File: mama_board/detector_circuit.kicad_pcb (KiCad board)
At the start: 4 copper layers, 94 x 99.1 mm, 123 parts, among them J1 Programming Header, J2 CAN Header, J3 BATT_1, J4 BATT_2, J5 BATT_3, J6 BATT_4, J7 TEST_CONN, J8 693072010801, J9 SIPM_CONN, Q1 BSS138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

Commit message: Addressed Jack's Comments, got half of Chamath's comments addressed
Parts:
- removed J2: CAN Header, Connector_PinHeader_2.54mm:PinHeader_1x05_P2.54mm_Vertical
- removed REF** (x4): MountingHole_3.5mm, MountingHole:MountingHole_3.5mm
- added J10: Conn_01x06_Female, canhw_footprints:connector_Harwin_M80-5000642, F.Cu at (105.0, 54.1)
- JP5: value TRANS_OUT -> TRANS_JUMP
- TP1: value PEAK OUT -> PEAK_OUT
- U3: footprint Package_TO_SOT_SMD:SOT-23-5_HandSoldering -> Package_TO_SOT_SMD:TSOT-23-5_HandSoldering
- moved L1 2.19 mm to (165.2, 100.6)
- moved C15 2.05 mm to (166.0, 106.9)
- moved C16 2.05 mm to (166.0, 109.9)
- moved D1 2.05 mm to (169.7, 105.4)
- moved C7 1.91 mm to (170.2, 100.6)
- moved R11 1.53 mm to (161.9, 111.6)
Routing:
- net +BATT: track 60.3 -> 38.3 mm
- net Net-(C7-Pad1): track 58.3 -> 42.0 mm
- net GND: track 203.8 -> 189.5 mm, vias 123 -> 127
- net +37V: track 32.7 -> 24.4 mm
- net /Microcontroller [DO NOT PLACE]/CANL: track 12.3 -> 8.32 mm
- net Net-(D1-Pad2): track 10.6 -> 12.1 mm
- net /Microcontroller [DO NOT PLACE]/CANH: track 7.13 -> 5.78 mm, vias 0 -> 1
- net Net-(R11-Pad1): track 6.55 -> 5.42 mm
- net Net-(J8-Pad3): track 15.4 -> 16.3 mm
- net Net-(C18-Pad2): track 35.2 -> 36.0 mm
- net Net-(R28-Pad2): track 23.5 -> 22.9 mm
- net +5V: track 91.9 -> 91.7 mm, vias 12 -> 15
- added copper zone on F.Cu, net +4.7V
- added copper zone on F.Cu, net +5V
- added copper zone on F.Cu, net +BATT
- added copper zone on F.Cu, net Net-(C7-Pad1)
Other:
- board text added: "CAN Header"

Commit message: Finished Addressing chamath's Reviews
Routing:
- net /AMP_OUT: track 46.1 -> 36.0 mm
- net +4.7V: track 80.1 -> 82.0 mm
- net GND: track 189.5 -> 191.1 mm
- added copper zone on F.Cu, net /AMP_OUT

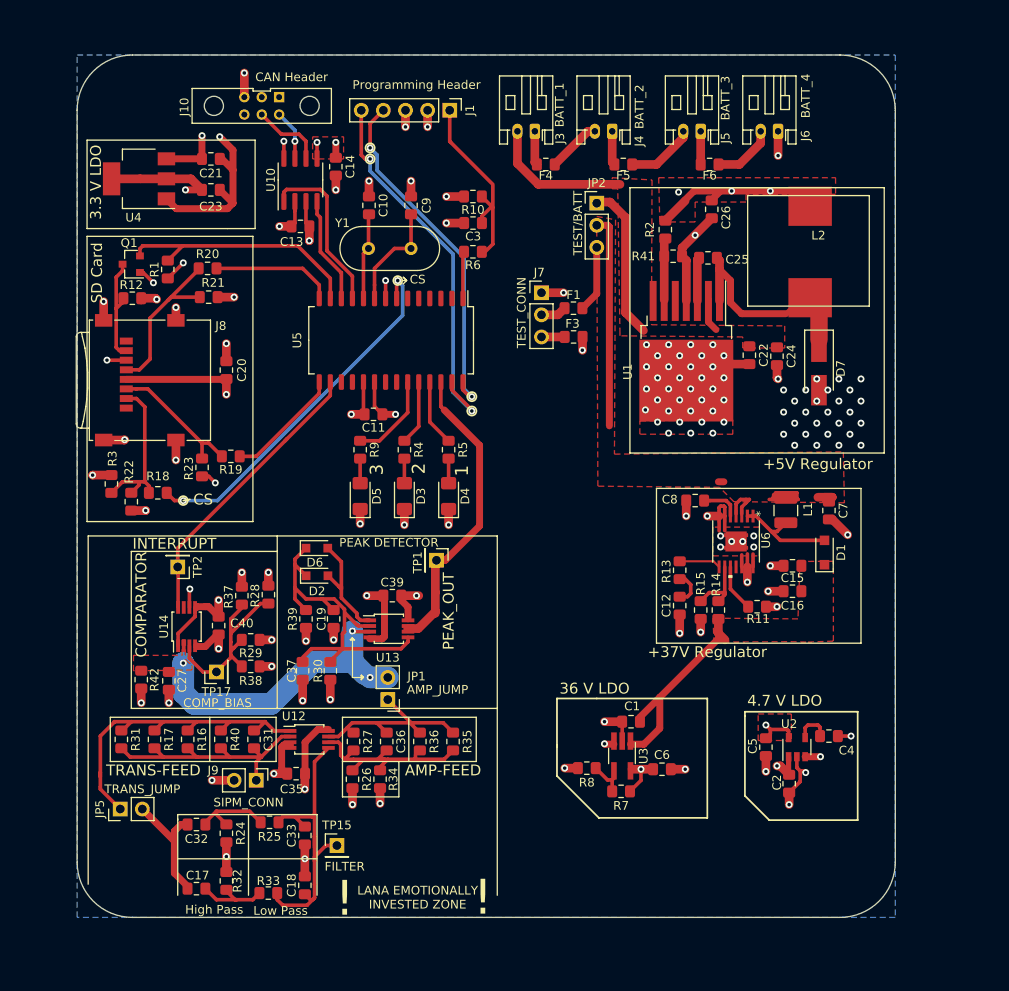
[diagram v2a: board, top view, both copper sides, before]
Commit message: added ground plane
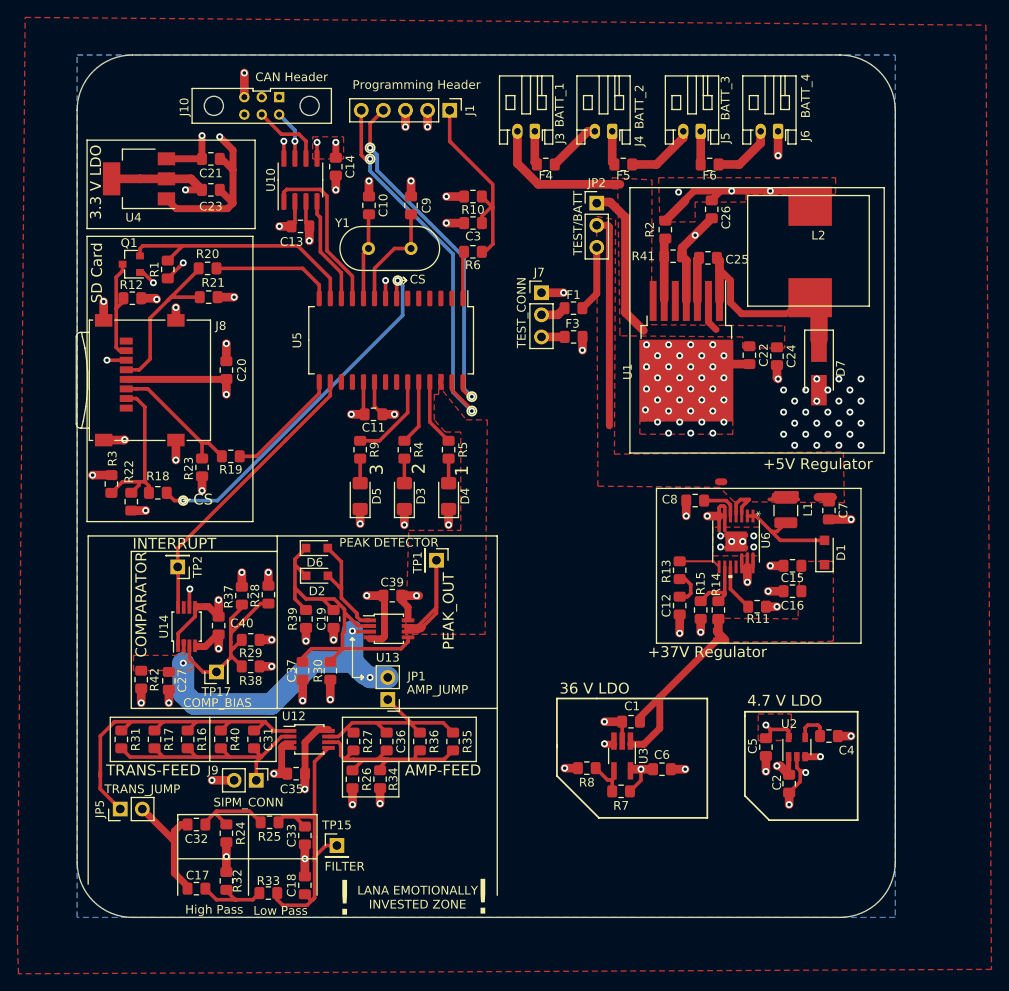
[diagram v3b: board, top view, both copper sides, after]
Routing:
- net /DET_ADC: track 35.0 -> 21.6 mm
- net +5V: track 91.7 -> 93.2 mm
- net GND: track 191.1 -> 190.5 mm
- added copper zone on F.Cu, net /DET_ADC
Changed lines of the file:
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@@
     (thickness 1.6)
     (drawings 110)
-    (tracks 881)
+    (tracks 879)
     (zones 0)
     (modules 119)
@@
   (layers
     (0 Papa.Cu signal)
-    (1 GND.Cu power hide)
-    (2 VCC.Cu power hide)
+    (1 GND.Cu power)
+    (2 VCC.Cu power)
     (31 Mama.Cu signal)
     (32 B.Adhes user hide)
@@
   )
   (setup
-    (last_trace_width 1)
+    (last_trace_width 0.8)
     (user_trace_width 0.42)
     (user_trace_width 0.8)
@@
   (via (at 144.399 124.841) (size 0.8) (drill 0.4) (layers Papa.Cu Mama.Cu) (net 1))
   (via (at 91.694 100.584) (size 0.8) (drill 0.4) (layers Papa.Cu Mama.Cu) (net 1))
-  (via (at 99.695 97.409) (size 0.8) (drill 0.4) (layers Papa.Cu Mama.Cu) (net 1))
-  (segment (start 98.171 96.656) (end 98.942 96.656) (width 0.42) (layer Papa.Cu) (net 1))
-  (segment (start 98.942 96.656) (end 99.695 97.409) (width 0.42) (layer Papa.Cu) (net 1))
+  (via (at 98.171 98.298) (size 0.8) (drill 0.4) (layers Papa.Cu Mama.Cu) (net 1))
   (via (at 100.965 81.407) (size 0.8) (drill 0.4) (layers Papa.Cu Mama.Cu) (net 1))
   (via (at 101.854 76.073) (size 0.8) (drill 0.4) (layers Papa.Cu Mama.Cu) (net 1))
@@
   (segment (start 166.878 131.717) (end 165.608 132.987) (width 0.42) (layer Papa.Cu) (net 1))
   (segment (start 166.878 130.498602) (end 166.878 131.717) (width 0.42) (layer Papa.Cu) (net 1))
-  (segment (start 171.205 126.492) (end 172.72 126.492) (width 0.42) (layer Papa.Cu) (net 1))
   (segment (start 144.399 124.841) (end 146.422 124.841) (width 1) (layer Papa.Cu) (net 1))
   (segment (start 121.412 100.4205) (end 121.412 102.235) (width 1) (layer Papa.Cu) (net 1))
@@
   (segment (start 108.839 65.086) (end 108.839 66.167) (width 0.42) (layer Papa.Cu) (net 1))
   (via (at 164.211 111.633) (size 0.8) (drill 0.4) (layers Papa.Cu Mama.Cu) (net 1))
-  (segment (start 170.18 101.609) (end 170.57 101.609) (width 1) (layer Papa.Cu) (net 1))
-  (segment (start 170.57 101.609) (end 172.339 103.378) (width 1) (layer Papa.Cu) (net 1))
-  (segment (start 172.339 103.378) (end 172.339 103.378) (width 1) (layer Papa.Cu) (net 1))
-  (via (at 172.339 103.378) (size 0.8) (drill 0.4) (layers Papa.Cu Mama.Cu) (net 1))
   (segment (start 162.95 111.633) (end 164.211 111.633) (width 1) (layer Papa.Cu) (net 1))
   (via (at 167.513 130.683) (size 0.8) (drill 0.4) (layers Papa.Cu Mama.Cu) (net 1))
@@
   (segment (start 94.361 121.176) (end 94.361 122.682) (width 1) (layer Papa.Cu) (net 1))
   (segment (start 100.076 114.826) (end 100.076 116.459) (width 1) (layer Papa.Cu) (net 1))
+  (segment (start 98.171 96.656) (end 98.171 98.298) (width 1) (layer Papa.Cu) (net 1))
+  (segment (start 170.18 101.609) (end 172.729 101.609) (width 1) (layer Papa.Cu) (net 1))
+  (segment (start 172.729 101.609) (end 172.729 101.609) (width 1) (layer Papa.Cu) (net 1))
+  (via (at 172.729 101.609) (size 0.8) (drill 0.4) (layers Papa.Cu Mama.Cu) (net 1))
+  (segment (start 171.205 126.492) (end 172.72 126.492) (width 1) (layer Papa.Cu) (net 1))
   (via (at 96.012 72.136) (size 0.8) (drill 0.4) (layers Papa.Cu Mama.Cu) (net 2))
   (via (at 98.171 57.531) (size 0.8) (drill 0.4) (layers Papa.Cu Mama.Cu) (net 2))
@@
   (segment (start 117.983 85.826) (end 117.983 88.628) (width 0.42) (layer Papa.Cu) (net 2))
   (segment (start 120.396 89.535) (end 120.396 89.535) (width 0.42) (layer Papa.Cu) (net 2))
-  (via (at 120.396 89.535) (size 0.8) (drill 0.4) (layers Papa.Cu Mama.Cu) (net 2))
+  (via (at 120.269 89.535) (size 0.8) (drill 0.4) (layers Papa.Cu Mama.Cu) (net 2))
   (segment (start 141.877 80.645) (end 141.877 82.187) (width 1) (layer Papa.Cu) (net 2))
   (segment (start 98.148 60.184) (end 98.162 60.198) (width 0.8) (layer Papa.Cu) (net 2))
@@
   (segment (start 163.449 63.881) (end 159.004 63.881) (width 0.8) (layer Papa.Cu) (net 2))
   (via (at 163.449 63.881) (size 0.8) (drill 0.4) (layers Papa.Cu Mama.Cu) (net 2))
+  (segment (start 120.307854 89.535) (end 120.351927 89.490927) (width 1) (layer Papa.Cu) (net 2))
+  (segment (start 118.89 89.535) (end 120.307854 89.535) (width 1) (layer Papa.Cu) (net 2))
   (segment (start 130.311 70.866) (end 130.683 70.866) (width 0.42) (layer Papa.Cu) (net 3))
   (segment (start 130.683 70.866) (end 131.572 69.977) (width 0.42) (layer Papa.Cu) (net 3))
@@
   (segment (start 101.473 114.681) (end 101.473 115.697) (width 0.42) (layer Papa.Cu) (net 53))
   (segment (start 101.473 113.03) (end 101.473 114.681) (width 0.42) (layer Papa.Cu) (net 53))
-  (segment (start 130.048 93.091) (end 125.984 89.027) (width 0.8) (layer Papa.Cu) (net 54))
-  (segment (start 125.603 88.646) (end 125.984 89.027) (width 0.42) (layer Papa.Cu) (net 54))
-  (segment (start 125.603 85.826) (end 125.603 88.646) (width 0.42) (layer Papa.Cu) (net 54))
-  (segment (start 124.968 106.426) (end 125.095 106.299) (width 1) (layer Papa.Cu) (net 54))
-  (segment (start 124.968 109.982) (end 124.968 106.426) (width 1) (layer Papa.Cu) (net 54))
-  (segment (start 124.968 109.982) (end 124.968 112.394) (width 1) (layer Papa.Cu) (net 54))
-  (segment (start 125.095 106.299) (end 126.111 106.299) (width 0.8) (layer Papa.Cu) (net 54))
-  (segment (start 130.048 102.362) (end 130.048 93.091) (width 0.8) (layer Papa.Cu) (net 54))
-  (segment (start 126.111 106.299) (end 130.048 102.362) (width 0.8) (layer Papa.Cu) (net 54))
-  (segment (start 124.991999 112.167801) (end 123.063 114.0968) (width 1) (layer Papa.Cu) (net 54))
-  (segment (start 122.9868 114.1476) (end 121.781799 114.1476) (width 1) (layer Papa.Cu) (net 54))
+  (segment (start 125.095 111.732) (end 125.095 106.299) (width 0.42) (layer Papa.Cu) (net 54))
+  (segment (start 122.979 113.848) (end 125.095 111.732) (width 0.42) (layer Papa.Cu) (net 54))
+  (segment (start 121.834 113.848) (end 122.979 113.848) (width 0.42) (layer Papa.Cu) (net 54))
+  (segment (start 125.095 112.382) (end 125.095 106.299) (width 0.42) (layer Papa.Cu) (net 54))
+  (segment (start 121.834 114.498) (end 122.979 114.498) (width 0.42) (layer Papa.Cu) (net 54))
+  (segment (start 123.501 113.976) (end 123.304 114.173) (width 0.8) (layer Papa.Cu) (net 54))
+  (segment (start 122.979 114.498) (end 123.501 113.976) (width 0.42) (layer Papa.Cu) (net 54))
+  (segment (start 123.501 113.976) (end 125.095 112.382) (width 0.42) (layer Papa.Cu) (net 54))
+  (segment (start 123.304 114.173) (end 121.793 114.173) (width 0.8) (layer Papa.Cu) (net 54))
   (segment (start 111.379 66.548) (end 111.379 65.086) (width 0.42) (layer Papa.Cu) (net 55))
   (segment (start 111.76 66.929) (end 111.379 66.548) (width 0.42) (layer Papa.Cu) (net 55))
@@
     )
   )
-  (zone (net 1) (net_name GND) (layer GND.Cu) (hatch edge 0.508)
-    (priority 2)
-    (connect_pads yes (clearance 0))
-    (min_thickness 0.254)
-    (fill yes (arc_segments 16) (thermal_gap 0.508) (thermal_bridge_width 0.508))
-    (polygon
-      (pts
-        (xy 179.07 148.59) (xy 81.28 148.59) (xy 81.28 46.99) (xy 179.07 45.72)
-      )
-    )
-  )
   (zone (net 2) (net_name +5V) (layer VCC.Cu) (hatch edge 0.508)
     (priority 2)
@@
   )
   (zone (net 1) (net_name GND) (layer Mama.Cu) (hatch edge 0.508)
-    (priority 2)
+    (priority 4)
     (connect_pads yes (clearance 0))
     (min_thickness 0.254)
@@
   )
   (zone (net 61) (net_name /AMP_OUT) (layer Papa.Cu) (hatch edge 0.508)
+    (priority 1)
     (connect_pads yes (clearance 0))
     (min_thickness 0.254)
@@
       )
     )
+  )
+  (zone (net 54) (net_name /DET_ADC) (layer Papa.Cu) (hatch edge 0.508)
+    (priority 1)
+    (connect_pads yes (clearance 0))
+    (min_thickness 0.254)
+    (fill yes (arc_segments 32) (thermal_gap 0.508) (thermal_bridge_width 0.508) (smoothing fillet) (radius 2))
+    (polygon
+      (pts
+        (xy 125.857 86.868) (xy 128.524 90.17) (xy 130.937 90.17) (xy 130.683 114.808) (xy 121.539 114.808)
+        (xy 121.92 102.87) (xy 127.889 102.87) (xy 127.889 91.567) (xy 126.111 91.567) (xy 124.841 90.17)
+        (xy 124.841 87.249) (xy 125.349 87.249) (xy 125.349 84.963) (xy 125.857 84.963)
+      )
+    )
+  )
+  (zone (net 1) (net_name GND) (layer GND.Cu) (hatch edge 0.508)
+    (connect_pads yes (clearance 0))
+    (min_thickness 0.254)
+    (fill yes (arc_segments 16) (thermal_gap 0.508) (thermal_bridge_width 0.508))
+    (polygon
+      (pts
+        (xy 179.705 150.241) (xy 82.042 150.241) (xy 82.423 47.371) (xy 179.197 47.371)
+      )
+    )
+  )
+  (zone (net 1) (net_name GND) (layer Papa.Cu) (hatch edge 0.508)
+    (connect_pads yes (clearance 0))
+    (min_thickness 0.254)
+    (fill yes (arc_segments 16) (thermal_gap 0.508) (thermal_bridge_width 0.508))
+    (polygon
+      (pts
+        (xy 188.214 44.831) (xy 188.849 153.289) (xy 77.089 153.797) (xy 76.962 149.987) (xy 77.851 43.942)
+      )
+    )

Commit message: addressed dawson & randy's comments, with the exception of team logo cause im having trouble
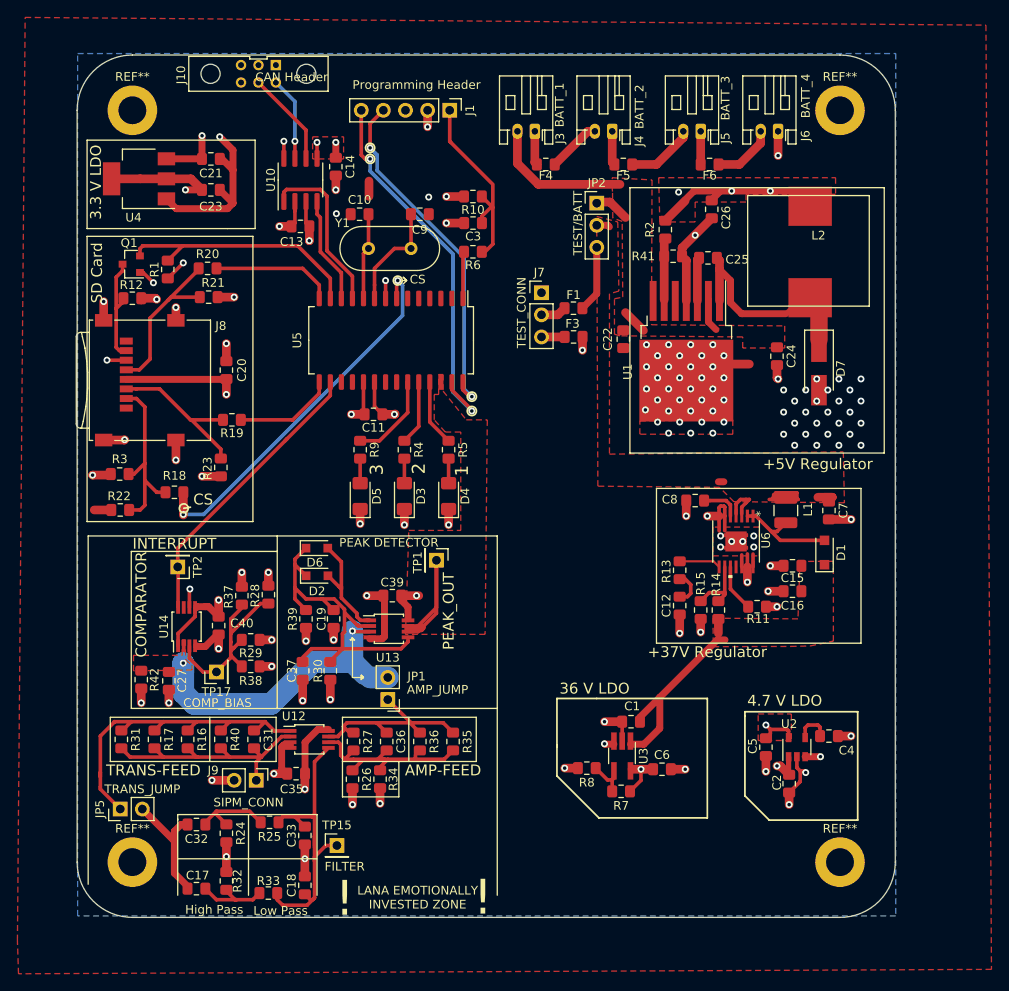
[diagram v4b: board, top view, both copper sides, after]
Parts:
- added REF**: MountingHole_3.2mm_M3_ISO7380_Pad, MountingHole:MountingHole_3.2mm_M3_ISO7380_Pad, F.Cu at (90.2, 54.6)
- added REF**: MountingHole_3.2mm_M3_ISO7380_Pad, MountingHole:MountingHole_3.2mm_M3_ISO7380_Pad, F.Cu at (171.4, 54.6)
- added REF**: MountingHole_3.2mm_M3_ISO7380_Pad, MountingHole:MountingHole_3.2mm_M3_ISO7380_Pad, F.Cu at (171.4, 141.0)
- added REF**: MountingHole_3.2mm_M3_ISO7380_Pad, MountingHole:MountingHole_3.2mm_M3_ISO7380_Pad, F.Cu at (90.2, 141.0)
- moved C22 14.6 mm to (146.6, 80.9)
- moved R19 4.19 mm to (101.6, 90.2)
- moved J10 3.70 mm to (104.6, 50.4)
- moved R23 2.16 mm to (100.3, 95.6)
- moved R18 1.91 mm to (95.0, 98.5)
- moved R22 1.59 mm to (88.8, 100.5), turned to 180 degrees
- moved R3 1.49 mm to (88.7, 96.4), turned to 0 degrees
- moved C10 1.48 mm to (116.3, 66.5), turned to 180 degrees
- moved C9 1.44 mm to (123.2, 66.5), turned to 0 degrees
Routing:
- net Net-(C7-Pad1): track 42.0 -> 19.1 mm
- net +BATT: track 38.3 -> 27.4 mm
- net GND: track 190.5 -> 181.8 mm, vias 127 -> 123
- net /Microcontroller [DO NOT PLACE]/CANH: track 5.78 -> 9.62 mm
- net /Microcontroller [DO NOT PLACE]/CANL: track 8.32 -> 11.0 mm
- net Net-(J8-Pad2): track 18.6 -> 21.2 mm
- net Net-(J8-Pad3): track 16.3 -> 18.4 mm
- net /Microcontroller [DO NOT PLACE]/MISO: track 42.5 -> 40.7 mm
- net +37V: track 24.4 -> 23.3 mm
- net /Microcontroller [DO NOT PLACE]/CS: track 42.6 -> 43.6 mm
- net Net-(C36-Pad1): track 23.3 -> 24.1 mm
- net /AMP_OUT: vias 3 -> 2

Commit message: Addressed Jared's comments
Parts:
- removed the REF** at (90.2, 54.6)
- removed the REF** at (171.4, 54.6)
- removed the REF** at (171.4, 141.0)
- removed the REF** at (90.2, 141.0)
- added G***: LOGO, Team_Logo:Logo_SilkScreen_15mm, F.Cu at (125.0, 137.7)
- added REF**: MountingHole_3.5mm_Pad, MountingHole:MountingHole_3.5mm_Pad, F.Cu at (90.2, 141.0)
- added REF**: MountingHole_3.5mm_Pad, MountingHole:MountingHole_3.5mm_Pad, F.Cu at (90.2, 54.6)
- added REF**: MountingHole_3.5mm_Pad, MountingHole:MountingHole_3.5mm_Pad, F.Cu at (171.4, 54.6)
- added REF**: MountingHole_3.5mm_Pad, MountingHole:MountingHole_3.5mm_Pad, F.Cu at (171.4, 141.0)
- moved C14 8.35 mm to (107.6, 55.2), turned to 0 degrees
- moved U10 2.79 mm to (107.4, 60.7), turned to 270 degrees
- moved R20 2.29 mm to (101.1, 73.0)
- moved C13 2.13 mm to (107.3, 67.9), turned to 0 degrees
- moved F3 1.91 mm to (140.9, 82.5)
- moved R14 1.49 mm to (158.8, 112.8)
- moved R10 1.47 mm to (129.1, 63.1)
- moved Q1 1.17 mm to (90.0, 71.1)
- moved R1 1.08 mm to (95.3, 73.0), turned to 180 degrees
- moved R13 0.99 mm to (152.4, 106.7)
- moved J4 0.76 mm to (146.1, 57.0)
- moved C3 0.70 mm to (129.2, 66.9)
- moved R41 0.65 mm to (152.1, 72.0)
- moved C12 0.64 mm to (152.4, 111.5)
- moved R7 0.63 mm to (146.3, 133.5)
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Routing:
- net /Microcontroller [DO NOT PLACE]/PIC_RX: track 12.3 -> 28.1 mm, vias 0 -> 2
- net /AMP_OUT: track 36.0 -> 47.0 mm
- net /Microcontroller [DO NOT PLACE]/CANH: track 9.62 -> 17.3 mm
- net GND: track 181.8 -> 175.2 mm, vias 123 -> 122
- net /Microcontroller [DO NOT PLACE]/CANL: track 11.0 -> 17.6 mm, vias 0 -> 1
- net Net-(R2-Pad2): track 7.74 -> 11.5 mm
- net +BATT: track 27.4 -> 30.6 mm
- net /Microcontroller [DO NOT PLACE]/PIC_TX: track 19.4 -> 22.3 mm, vias 0 -> 1
- net /Microcontroller [DO NOT PLACE]/SCK: track 14.1 -> 11.9 mm
- net +37V: track 23.3 -> 21.6 mm
- net Net-(C12-Pad1): track 3.97 -> 5.61 mm
- net +3V3: track 32.3 -> 33.9 mm, vias 5 -> 4
- net Net-(R14-Pad2): track 7.40 -> 8.83 mm
- net +36V: track 63.0 -> 64.3 mm
- net Net-(J8-Pad7): track 12.3 -> 13.5 mm
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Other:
- board text added: "Artem Sotnikov"
- board text added: "DO"
- board text added: "Lana Tomlin"
- board text added: "Mount Vesuvius"
- board text added: "NOT"
- board text added: "PLACE"
- board text removed: "CS"

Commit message: Made polygons thermal, removed pours from under inductors, generated gerbers, did more silkscreen fine tuning
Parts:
- moved G*** 1.02 mm to (124.1, 138.2)
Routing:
- net GND: track 175.2 -> 151.6 mm, vias 122 -> 125
- net Net-(C7-Pad1): track 19.1 -> 7.05 mm
- net /DET_ADC: track 21.6 -> 10.1 mm
- net +5V: track 92.7 -> 81.6 mm
- net +37V: track 21.6 -> 25.7 mm
- net +BATT: track 30.6 -> 28.4 mm
- net /AMP_OUT: track 47.0 -> 49.1 mm
- net /Microcontroller [DO NOT PLACE]/MCLR: track 22.9 -> 22.1 mm
- net Net-(J8-Pad7): track 13.5 -> 14.1 mm
